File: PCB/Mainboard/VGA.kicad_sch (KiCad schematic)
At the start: 98 parts, among them J2 LCD_Connector, Q1 IS6, Q2 8C, U51 CHIPS65535

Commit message: Add files via upload
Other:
- company: (none) -> Recreated by: Ahmad Byagowi
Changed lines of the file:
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@@
 	(title_block
 		(title "PC110")
+		(company "Recreated by: Ahmad Byagowi")
 	)
 	(junction

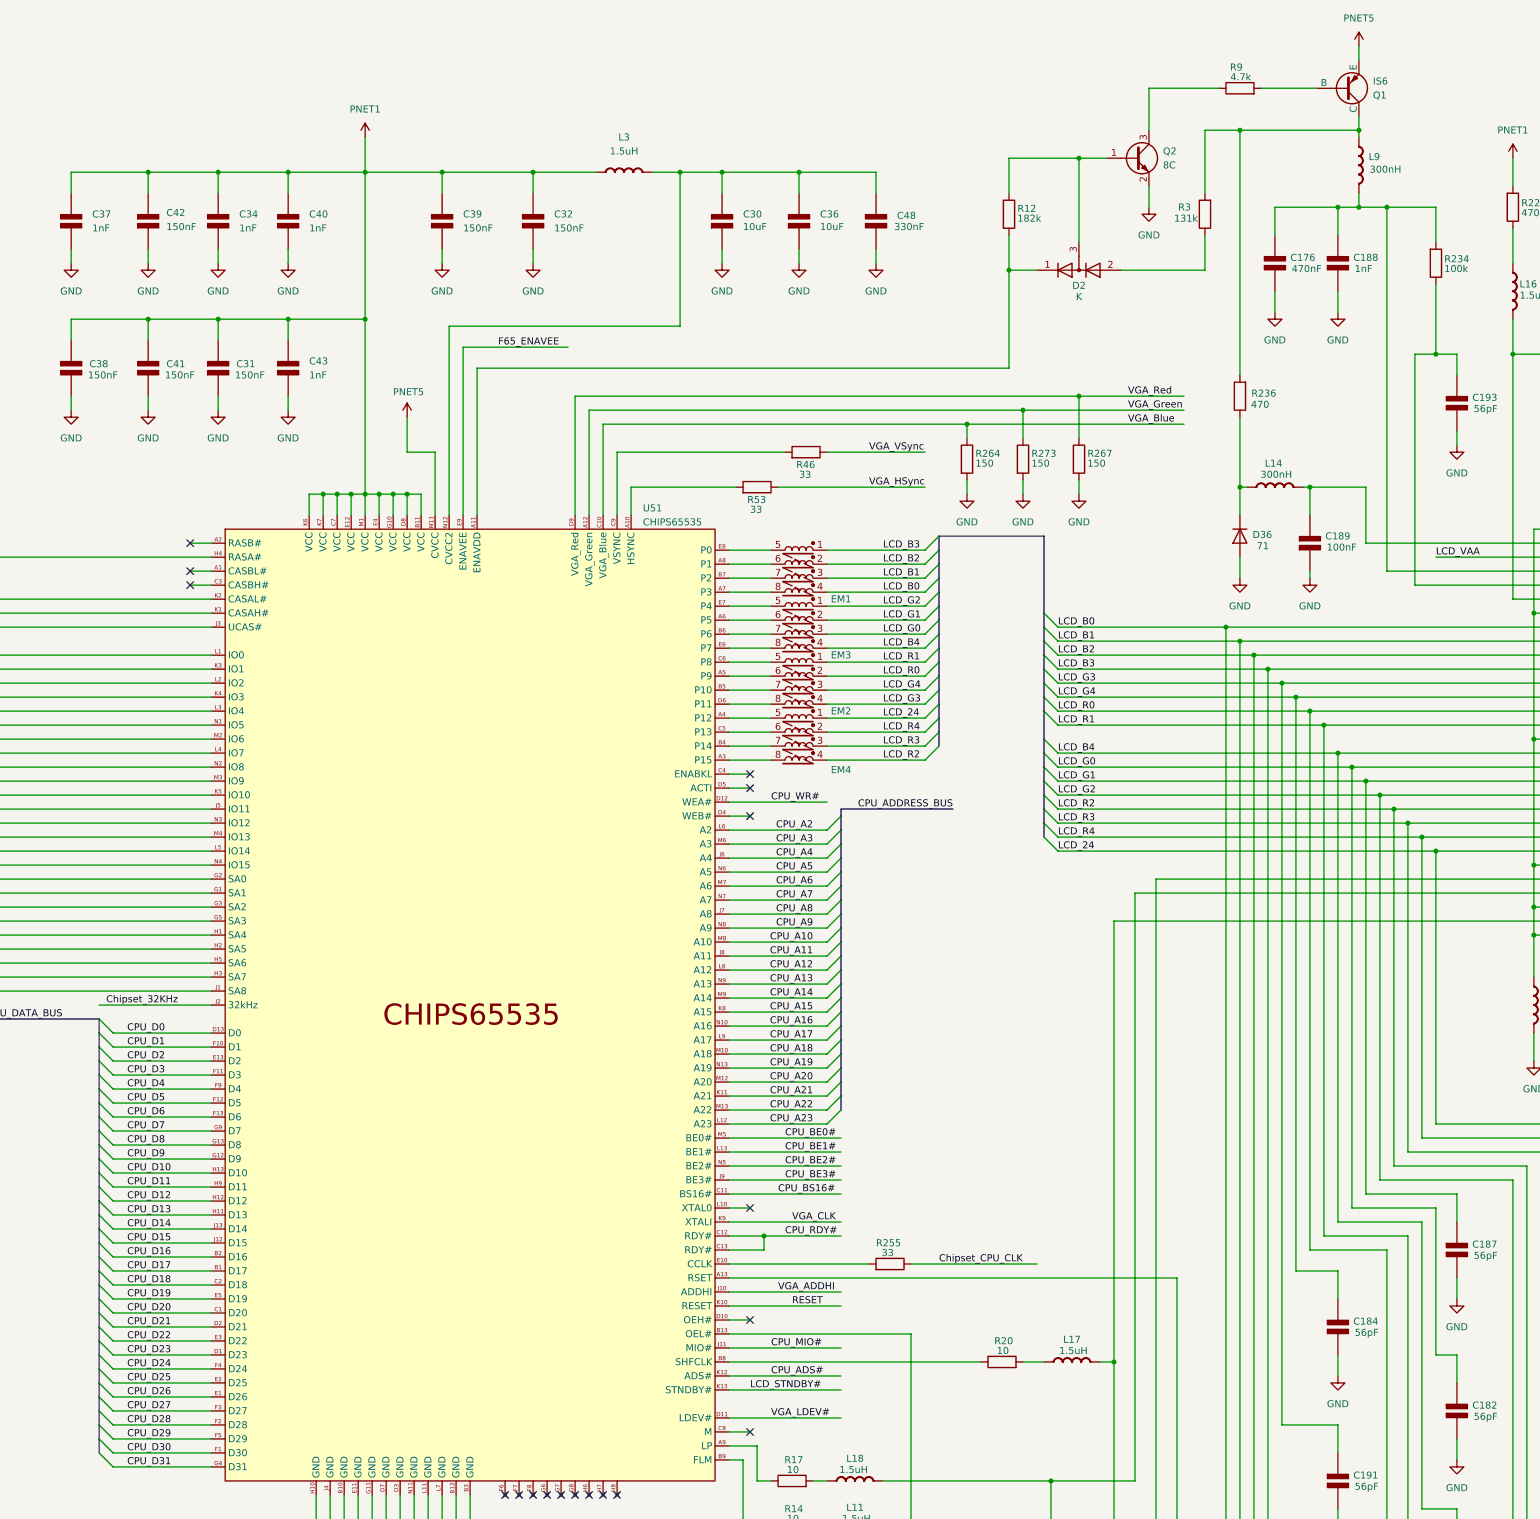
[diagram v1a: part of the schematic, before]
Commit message: Add part numbers to some SMT parts
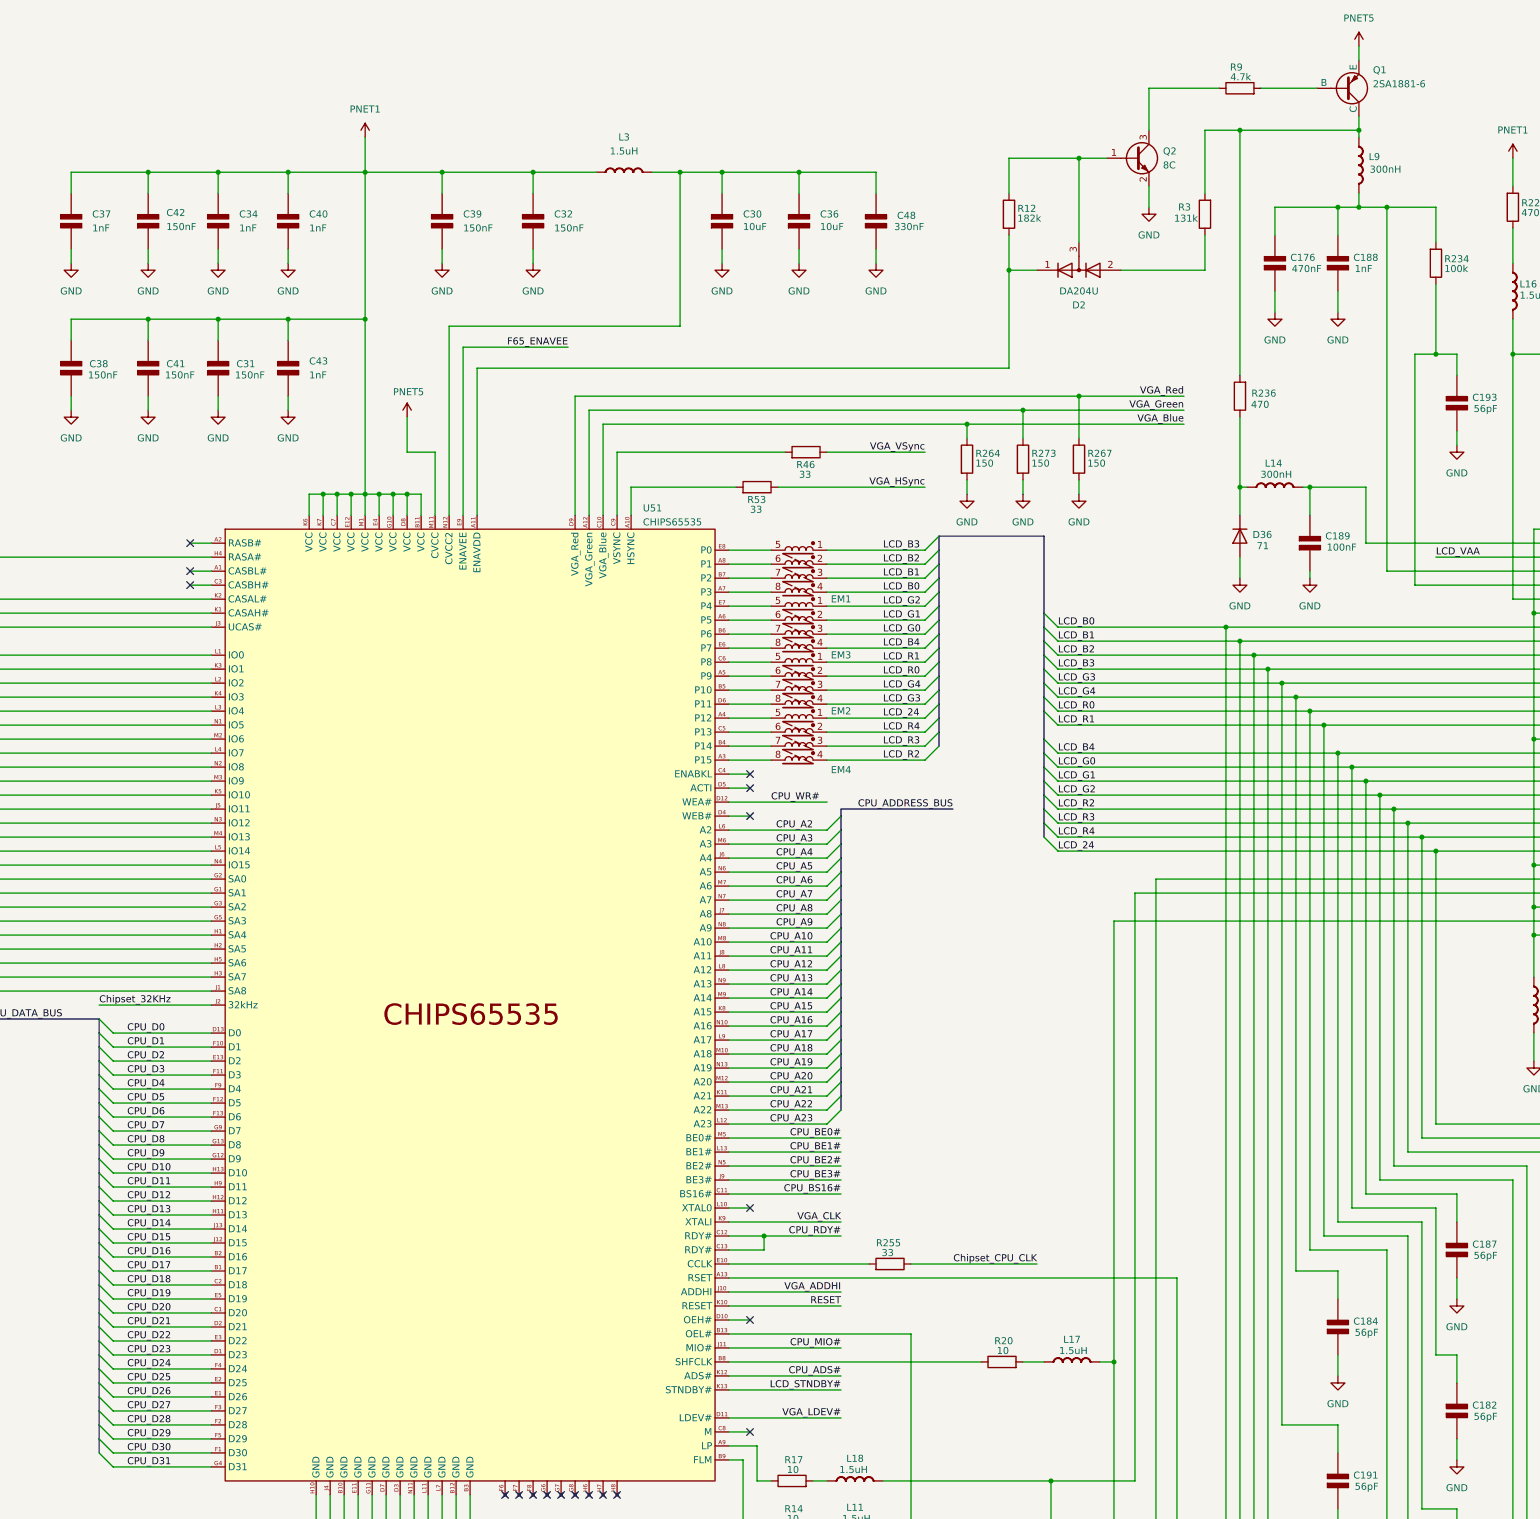
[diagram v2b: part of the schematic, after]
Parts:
- D2: value K -> DA204U; Topmark (none) -> K
- Q1: value IS6 -> 2SA1881-6; Topmark (none) -> IS6
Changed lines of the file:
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@@
 	)
 	(label "CPU_BE1#"
-		(at 416.56 226.06 0)
+		(at 426.72 226.06 180)
 		(effects
 			(font
 				(size 1.27 1.27)
 			)
-			(justify left bottom)
+			(justify right bottom)
 		)
 	)
@@
 	)
 	(label "F65_ENAVEE"
-		(at 364.49 80.01 0)
+		(at 377.19 80.01 180)
 		(effects
 			(font
 				(size 1.27 1.27)
 			)
-			(justify left bottom)
+			(justify right bottom)
 		)
 	)
 	(label "CPU_MIO#"
-		(at 414.02 261.62 0)
+		(at 426.72 261.62 180)
 		(effects
 			(font
 				(size 1.27 1.27)
 			)
-			(justify left bottom)
+			(justify right bottom)
 		)
 	)
@@
 	)
 	(label "VGA_CLK"
-		(at 417.83 238.76 0)
+		(at 426.72 238.76 180)
 		(effects
 			(font
 				(size 1.27 1.27)
 			)
-			(justify left bottom)
+			(justify right bottom)
 		)
 	)
@@
 	)
 	(label "CPU_BE0#"
-		(at 416.56 223.52 0)
+		(at 426.72 223.52 180)
 		(effects
 			(font
 				(size 1.27 1.27)
 			)
-			(justify left bottom)
+			(justify right bottom)
 		)
 	)
@@
 	)
 	(label "LCD_STNDBY#"
-		(at 410.21 269.24 0)
+		(at 426.72 269.24 180)
 		(effects
 			(font
 				(size 1.27 1.27)
 			)
-			(justify left bottom)
+			(justify right bottom)
 		)
 	)
 	(label "VGA_VSync"
-		(at 431.8 99.06 0)
+		(at 441.96 99.06 180)
 		(effects
 			(font
 				(size 1.27 1.27)
 			)
-			(justify left bottom)
+			(justify right bottom)
 		)
 	)
@@
 	)
 	(label "Chipset_32KHz"
-		(at 293.37 199.39 0)
+		(at 292.1 199.39 0)
 		(effects
 			(font
@@
 	)
 	(label "CPU_ADS#"
-		(at 414.02 266.7 0)
+		(at 426.72 266.7 180)
 		(effects
 			(font
 				(size 1.27 1.27)
 			)
-			(justify left bottom)
+			(justify right bottom)
 		)
 	)
@@
 	)
 	(label "CPU_BE3#"
-		(at 416.56 231.14 0)
+		(at 426.72 231.14 180)
 		(effects
 			(font
 				(size 1.27 1.27)
 			)
-			(justify left bottom)
+			(justify right bottom)
 		)
 	)
@@
 	)
 	(label "VGA_Blue"
-		(at 478.79 93.98 0)
+		(at 488.95 93.98 180)
 		(effects
 			(font
 				(size 1.27 1.27)
 			)
-			(justify left bottom)
+			(justify right bottom)
 		)
 	)
 	(label "CPU_RDY#"
-		(at 416.56 241.3 0)
+		(at 426.72 241.3 180)
 		(effects
 			(font
 				(size 1.27 1.27)
 			)
-			(justify left bottom)
+			(justify right bottom)
 		)
 	)
@@
 	)
 	(label "VGA_Green"
-		(at 478.79 91.44 0)
+		(at 488.95 91.44 180)
 		(effects
 			(font
 				(size 1.27 1.27)
 			)
-			(justify left bottom)
+			(justify right bottom)
 		)
 	)
@@
 	)
 	(label "VGA_HSync"
-		(at 431.8 105.41 0)
+		(at 441.96 105.41 180)
 		(effects
 			(font
 				(size 1.27 1.27)
 			)
-			(justify left bottom)
+			(justify right bottom)
 		)
 	)
@@
 	)
 	(label "VGA_Red"
-		(at 478.79 88.9 0)
+		(at 488.95 88.9 180)
 		(effects
 			(font
 				(size 1.27 1.27)
 			)
-			(justify left bottom)
+			(justify right bottom)
 		)
 	)
@@
 	)
 	(label "VGA_ADDHI"
-		(at 415.29 251.46 0)
+		(at 426.72 251.46 180)
 		(effects
 			(font
 				(size 1.27 1.27)
 			)
-			(justify left bottom)
+			(justify right bottom)
 		)
 	)
 	(label "Chipset_CPU_CLK"
-		(at 444.5 246.38 0)
+		(at 462.28 246.38 180)
 		(effects
 			(font
 				(size 1.27 1.27)
 			)
-			(justify left bottom)
+			(justify right bottom)
 		)
 	)
@@
 	)
 	(label "CPU_BE2#"
-		(at 416.56 228.6 0)
+		(at 426.72 228.6 180)
 		(effects
 			(font
 				(size 1.27 1.27)
 			)
-			(justify left bottom)
+			(justify right bottom)
 		)
 	)
@@
 	)
 	(label "CPU_BS16#"
-		(at 415.29 233.68 0)
+		(at 426.72 233.68 180)
 		(effects
 			(font
 				(size 1.27 1.27)
 			)
-			(justify left bottom)
+			(justify right bottom)
 		)
 	)
@@
 	)
 	(label "RESET"
-		(at 417.83 254 0)
+		(at 426.72 254 180)
 		(effects
 			(font
 				(size 1.27 1.27)
 			)
-			(justify left bottom)
+			(justify right bottom)
 		)
 	)
@@
 	)
 	(label "VGA_LDEV#"
-		(at 414.02 274.32 0)
+		(at 426.72 274.32 180)
 		(effects
 			(font
 				(size 1.27 1.27)
 			)
-			(justify left bottom)
+			(justify right bottom)
 		)
 	)
@@
 	)
 	(symbol
+		(lib_id "Device:D_Dual_Series_KAC")
+		(at 469.9 66.04 180)
+		(unit 1)
+		(exclude_from_sim no)
+		(in_bom yes)
+		(on_board yes)
+		(dnp no)
+		(property "Reference" "D2"
+			(at 469.9 72.39 0)
+			(effects
+				(font
+					(size 1.27 1.27)
+				)
+			)
+		)
+		(property "Value" "DA204U"
+			(at 469.9 69.85 0)
+			(effects
+				(font
+					(size 1.27 1.27)
+				)
+			)
+		)
+		(property "Footprint" ""
+			(at 469.9 66.04 0)
+			(effects
+				(font
+					(size 1.27 1.27)
+				)
+				(hide yes)
+			)
+		)
+		(property "Datasheet" "~"
+			(at 469.9 66.04 0)
+			(effects
+				(font
+					(size 1.27 1.27)
+				)
+				(hide yes)
+			)
+		)
+		(property "Description" "Dual diode, cathode/anode/center"
+			(at 469.9 66.04 0)
+			(effects
+				(font
+					(size 1.27 1.27)
+				)
+				(hide yes)
+			)
+		)
+		(property "Topmark" "K"
+			(at 469.9 66.04 0)
+			(effects
+				(font
+					(size 1.27 1.27)
+				)
+				(hide yes)
+			)
+		)
+		(pin "2"
+		)
+		(pin "3"
+		)
+		(pin "1"
+		)
+		(instances
+			(project "PC110"
+				(path "/45c7911f-b027-440e-9e3e-77a146b41944/00000000-0000-0000-0000-000066b27913"
+					(reference "D2")
+					(unit 1)
+				)
+			)
+		)
+	)
+	(symbol
 		(lib_id "Device:R")
 		(at 499.11 33.02 90)
@@
 		(dnp no)
 		(property "Reference" "Q1"
-			(at 523.24 34.2901 0)
+			(at 523.24 29.718 0)
 			(effects
 				(font
@@
 			)
 		)
-		(property "Value" "IS6"
-			(at 523.24 31.7501 0)
+		(property "Value" "2SA1881-6"
+			(at 523.24 32.258 0)
 			(effects
 				(font
@@
 			)
 		)
+		(property "Topmark" "IS6"
+			(at 518.16 33.02 0)
+			(effects
+				(font
+					(size 1.27 1.27)
+				)
+				(hide yes)
+			)
+		)
 		(pin "2"
 		)
@@
 					(unit 1)
 				)
-			)
-		)
-	)
-	(symbol
-		(lib_id "Device:D_Dual_Series_KAC")
-		(at 469.9 66.04 180)
-		(unit 1)
-		(exclude_from_sim no)
-		(in_bom yes)
-		(on_board yes)
-		(dnp no)
-		(property "Reference" "D2"
-			(at 469.9 68.834 0)
-			(effects
-				(font
-					(size 1.27 1.27)
-				)
-			)
-		)
-		(property "Value" "K"
-			(at 469.9 70.866 0)
-			(effects
-				(font
-					(size 1.27 1.27)
-				)
-			)
-		)
-		(property "Footprint" ""
-			(at 469.9 66.04 0)
-			(effects
-				(font
-					(size 1.27 1.27)
-				)
-				(hide yes)
-			)
-		)
-		(property "Datasheet" "~"
-			(at 469.9 66.04 0)
-			(effects
-				(font
-					(size 1.27 1.27)
-				)
-				(hide yes)
-			)
-		)
-		(property "Description" "Dual diode, cathode/anode/center"
-			(at 469.9 66.04 0)
-			(effects
-				(font
-					(size 1.27 1.27)
-				)
-				(hide yes)
-			)
-		)
-		(pin "2"
-		)
-		(pin "3"
-		)
-		(pin "1"
-		)
-		(instances
-			(project "PC110"
-				(path "/45c7911f-b027-440e-9e3e-77a146b41944/00000000-0000-0000-0000-000066b27913"
-					(reference "D2")
-					(unit 1)
-				)
